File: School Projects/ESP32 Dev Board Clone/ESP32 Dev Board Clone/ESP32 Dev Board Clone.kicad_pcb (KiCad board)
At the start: 2 copper layers, 53 x 68.1 mm, 53 parts, among them J2 Conn_01x06_Pin, J3 Barrel_Jack, P1 USB_C_Plug_USB2.0, Q1 PMOS, Q2 PMOS, Q3 PMOS, U2 CP2102N-Axx-xQFN24, U3 AMS1117-3.3

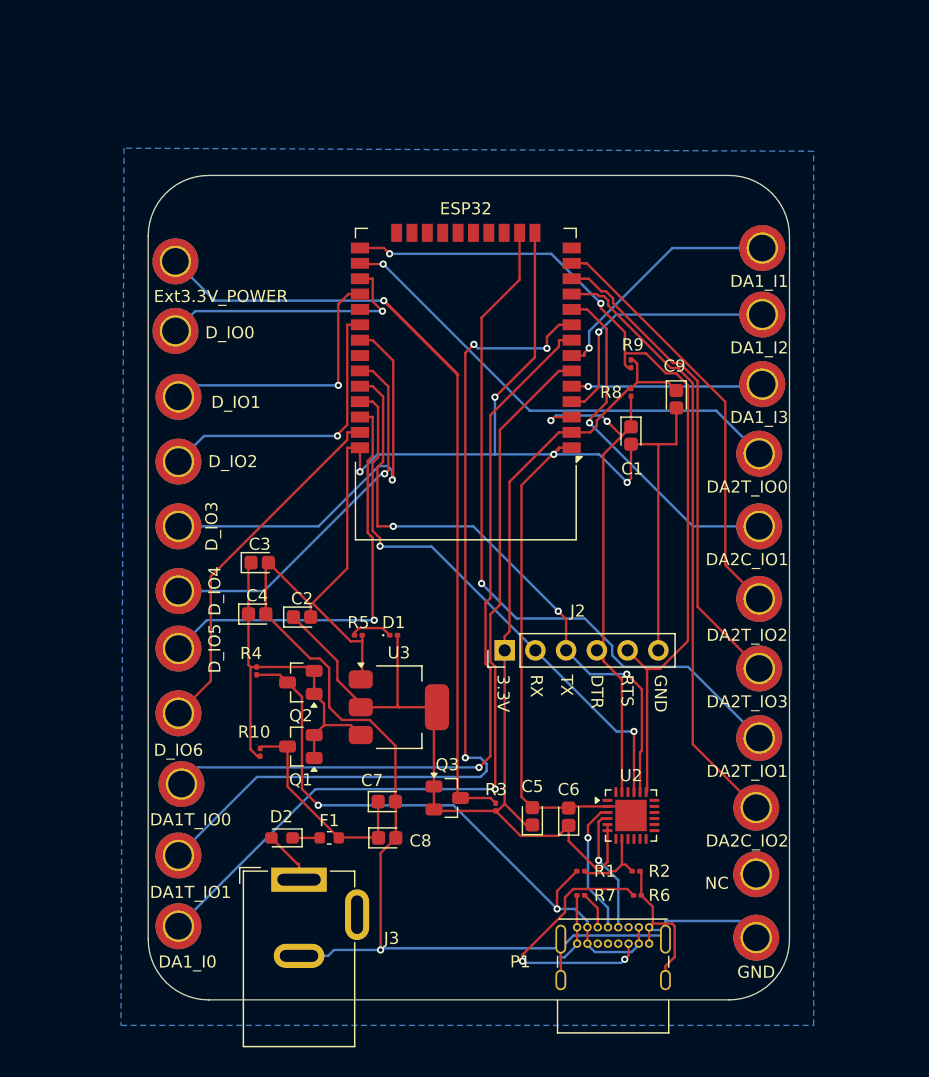
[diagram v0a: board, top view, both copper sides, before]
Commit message: Fully functioning esp32 clone board with pcb prod files
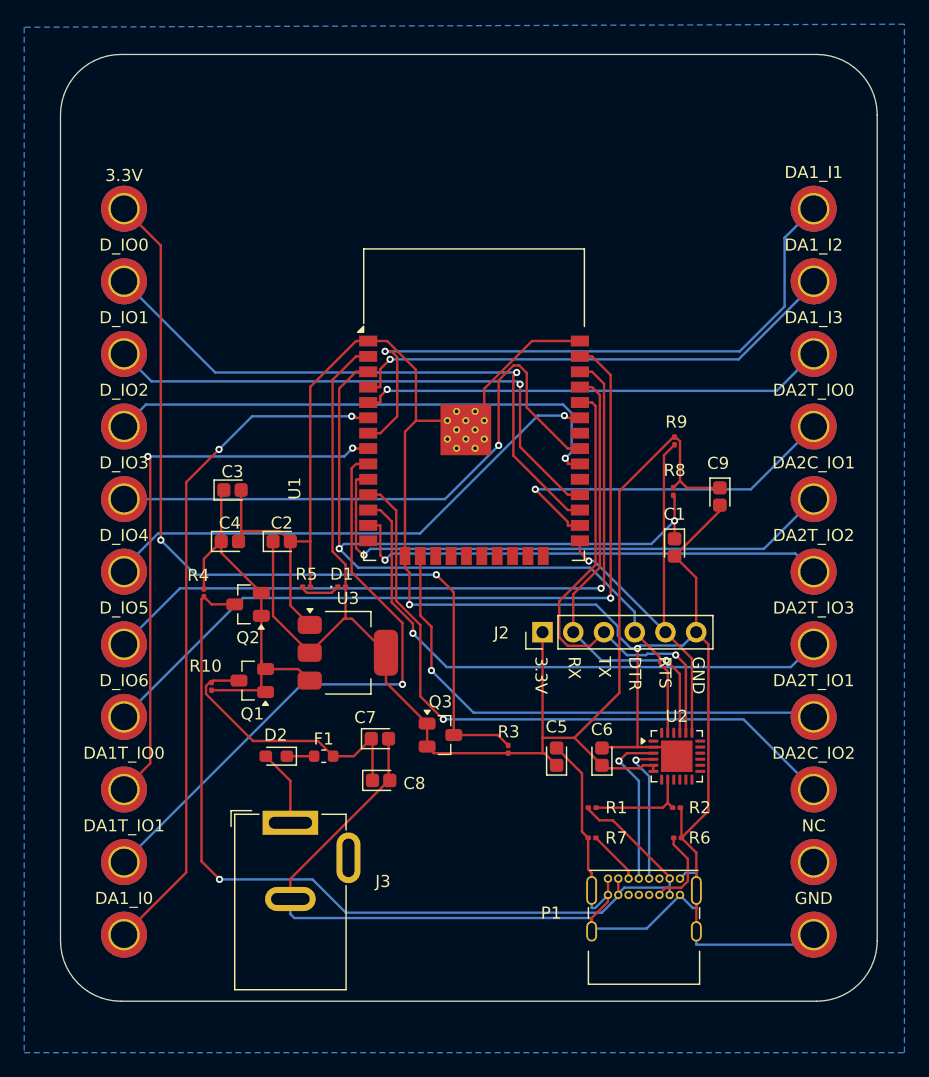
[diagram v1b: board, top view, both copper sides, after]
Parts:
- removed ESP32: ESP32, RF_Module:ESP32-WROOM-32
- added U1: ESP32-WROOM-32, RF_Module:ESP32-WROOM-32, F.Cu at (179.4, 66.7)
- H2: value Ext3.3V_POWER -> 3.3V
- moved C1 9.93 mm to (196.0, 75.5)
- moved R8 8.91 mm to (195.9, 70.9)
- moved C9 8.81 mm to (199.8, 71.3)
- moved Q2 7.79 mm to (160.8, 80.2)
- moved R4 7.79 mm to (157.1, 79.2)
- moved R9 7.32 mm to (196.0, 66.7)
- moved Q1 6.77 mm to (161.1, 86.5)
- moved R10 6.77 mm to (157.7, 87.0)
- moved D2 6.77 mm to (163.1, 92.8)
- moved F1 6.77 mm to (167.0, 92.8)
- moved C2 6.47 mm to (163.5, 75.0)
- moved C3 6.41 mm to (159.5, 70.8)
- moved C4 6.41 mm to (159.2, 75.0)
- moved R2 6.22 mm to (196.2, 97.0)
- moved U2 6.19 mm to (196.2, 92.8)
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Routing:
- net /DTR_EN: track 43.4 -> 86.2 mm
- net /RTS_IO0: track 72.5 -> 35.9 mm, vias 2 -> 1
- net /D_IO6: track 30.0 -> 65.9 mm, vias 0 -> 1
- net /DA1_I1: track 21.3 -> 52.7 mm
- net /D_IO0: track 22.1 -> 49.9 mm
- net /USB_POWER: track 52.2 -> 78.2 mm, vias 2 -> 1
- net /D_IO5: track 35.6 -> 60.8 mm
- net GND: track 250.2 -> 275.0 mm, vias 5 -> 2
- net /DA1T_IO1: track 75.0 -> 50.2 mm, vias 3 -> 1
- net /DA1_I3: track 15.8 -> 38.9 mm
- net /D_IO1: track 22.9 -> 45.5 mm
- net /DA1_I2: track 21.4 -> 41.5 mm
- net /D_IO2: track 24.6 -> 43.5 mm
- net /Vcc3.3V_POWER: track 102.6 -> 120.9 mm
- net /DA1T_IO0: track 65.0 -> 47.0 mm, vias 1 -> 2
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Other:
- board size 53 x 68.1 mm -> 67.5 x 78.2 mm
